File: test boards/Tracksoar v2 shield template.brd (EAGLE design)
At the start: 44.2 x 19.6 mm, 15 parts, among them J1 Analog 1, J2 Analog 0, J3 Digital IO 9, J4 Digital IO 8, J5 I2C, J6 SPI

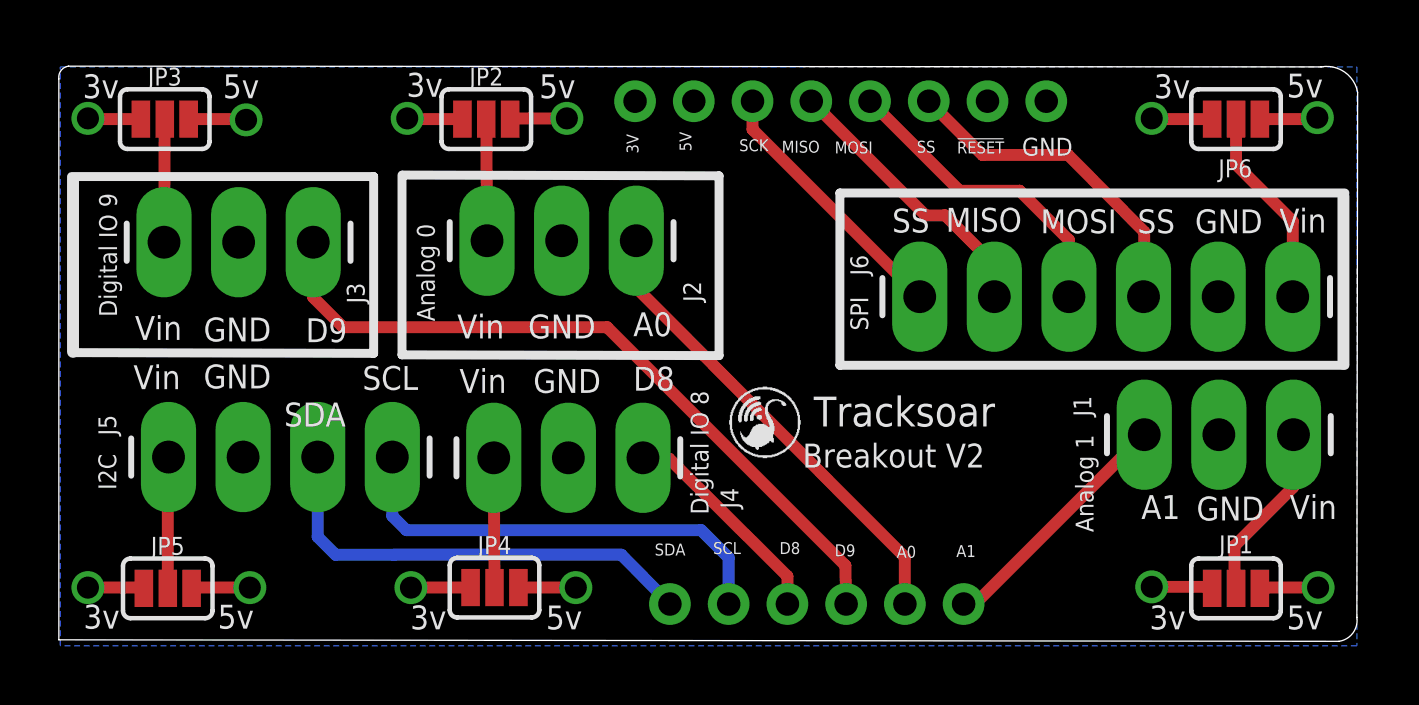
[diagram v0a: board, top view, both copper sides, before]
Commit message: fixed the v2 shield template
renamed the breakout board and re-added the template.
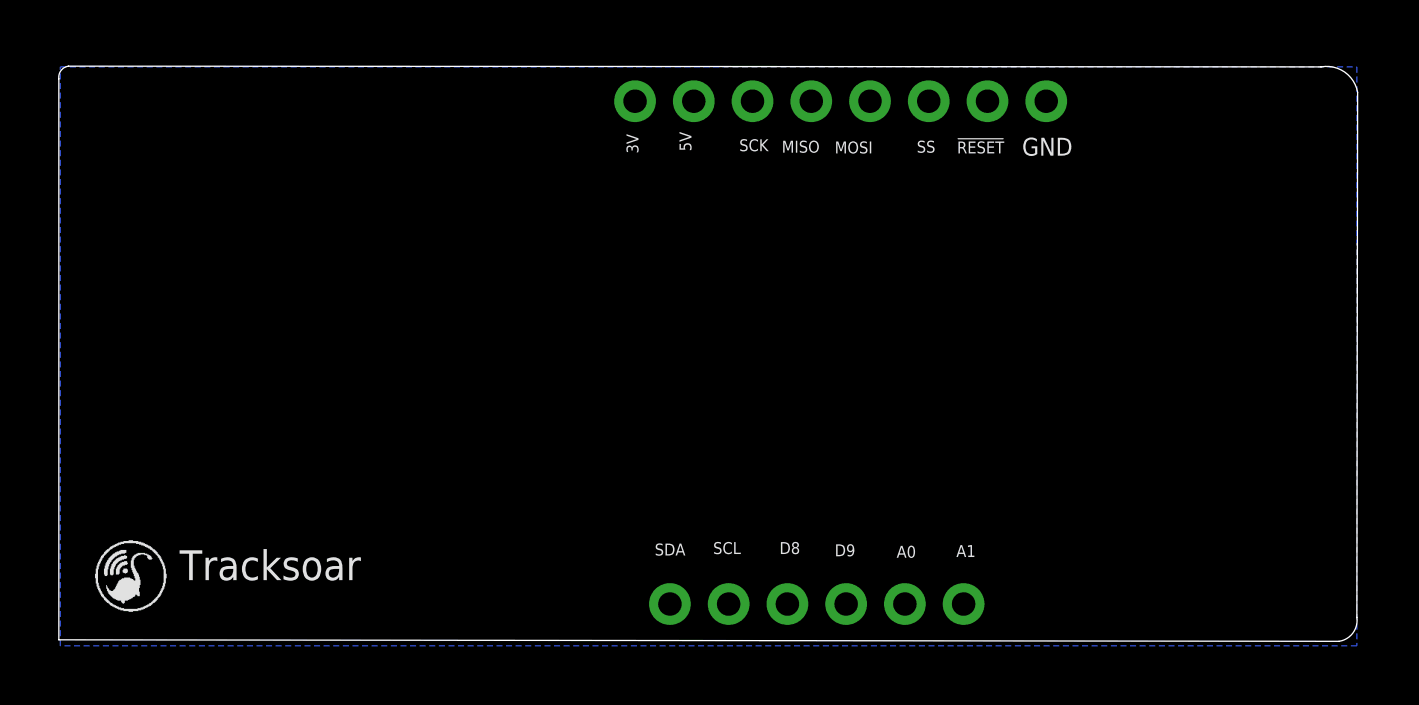
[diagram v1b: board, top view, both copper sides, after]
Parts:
- removed J1: Analog 1, SparkFun-Connectors:1X03_LONGPADS
- removed J2: Analog 0, SparkFun-Connectors:1X03_LONGPADS
- removed J3: Digital IO 9, SparkFun-Connectors:1X03_LONGPADS
- removed J4: Digital IO 8, SparkFun-Connectors:1X03_LONGPADS
- removed J5: I2C, SparkFun-Connectors:1X04_LONGPADS
- removed J6: SPI, SparkFun-Connectors:1X06_LONGPADS
- removed JP1, JP2, JP3, JP4, JP5, JP6: JUMPER-SMT_3_1-NC_PASTE_SILK, SparkFun-Jumpers:SMT-JUMPER_3_1-NC_PASTE_SILK
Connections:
- removed net N$1: J1.1, JP1.2
- removed net N$2: J2.1, JP2.2
- removed net N$3: J3.1, JP3.2
- removed net N$6: J4.1, JP4.2
- removed net N$7: J5.1, JP5.2
- removed net N$8: J6.1, JP6.2
- net 3V: no longer JP1.1, JP2.1, JP3.1, JP4.1, JP5.1, JP6.1
- net A0: no longer J2.3
- net A1: no longer J1.3
- net D8: no longer J4.3
- net D9: no longer J3.3
- net GND: no longer J1.2, J2.2, J3.2, J4.2, J5.2, J6.2
- net MISO: no longer J6.5
- net MOSI: no longer J6.4
- net SCK: no longer J6.6
- net SCL: no longer J5.4
- net SDA: no longer J5.3
- net SS: no longer J6.3
- net VCC: no longer JP1.3, JP2.3, JP3.3, JP4.3, JP5.3, JP6.3
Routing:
- net D9: track 25.1 -> 0.00 mm
- net A0: track 16.2 -> 0.00 mm
- net SDA: track 15.7 -> 0.00 mm
- net SCL: track 15.6 -> 0.00 mm
- net VCC: track 11.8 -> 0.00 mm, vias 6 -> 0
- net 3V: track 11.8 -> 0.00 mm, vias 6 -> 0
- net SS: track 11.4 -> 0.00 mm
- net MOSI: track 10.7 -> 0.00 mm
- net MISO: track 9.63 -> 0.00 mm
- net SCK: track 9.01 -> 0.00 mm
- net A1: track 8.54 -> 0.00 mm
- net D8: track 7.52 -> 0.00 mm
- net N$8: track 6.84 -> 0.00 mm
- net N$1: track 6.08 -> 0.00 mm
- net N$7: track 4.47 -> 0.00 mm
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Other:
- board text removed: "3v"
- board text removed: "5v"
- board text removed: "Breakout V2"
- board text removed: "Vin"
